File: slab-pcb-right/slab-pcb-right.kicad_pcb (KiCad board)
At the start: 2 copper layers, 158 x 104 mm, 147 parts, among them J1 Conn_01x04, J2 Conn_01x04, J3 TRRS_L, J4 TRRS_R, J5 SSD1306, SW1 RotaryEncoder, U1 Seeeduino Xiao rp2040, U2 PCA9555PW, U3 PCA9555PW, U4 ADS1110, U5 SN74AHCT125PWR, U6 TCA4307DGKR

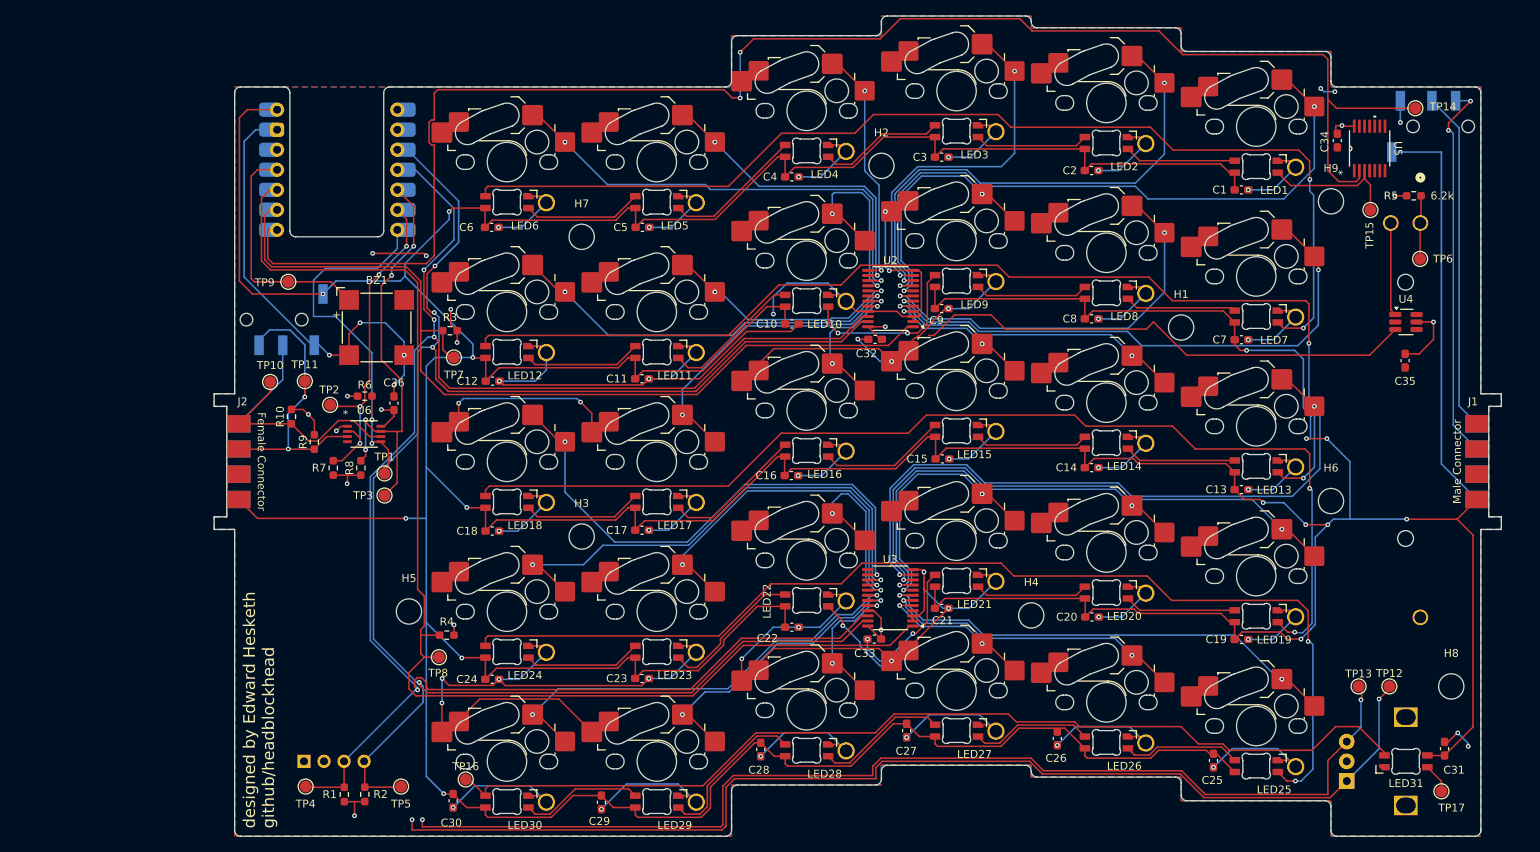
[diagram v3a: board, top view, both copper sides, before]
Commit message: feat: restart slab-pcb-right routing, allign components
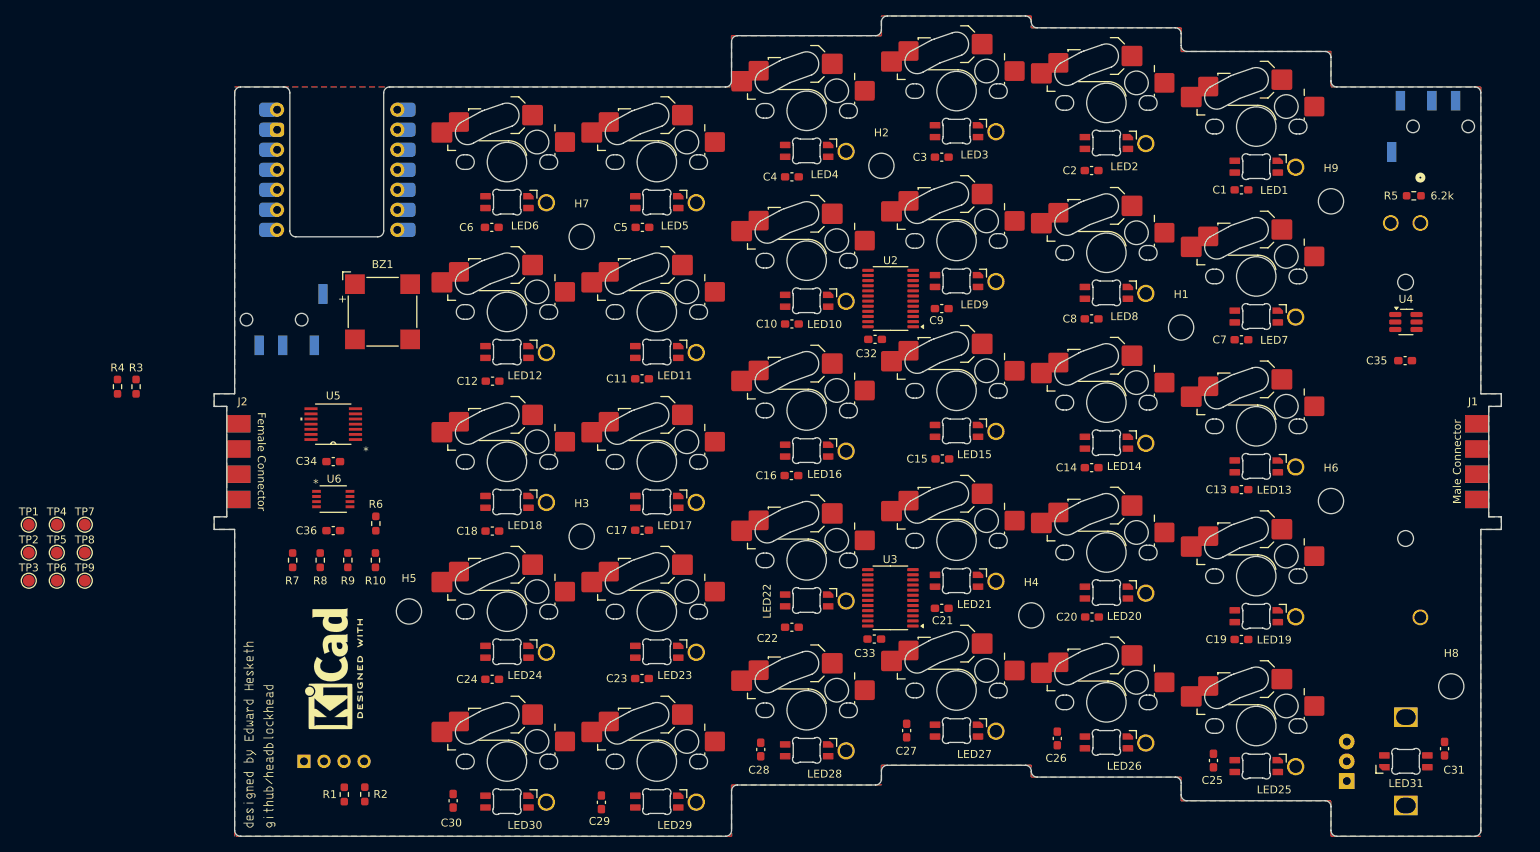
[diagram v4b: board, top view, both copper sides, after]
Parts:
- removed TP10, TP11, TP12, TP13, TP14, TP15, TP16, TP17: TestPoint, TestPoint:TestPoint_Pad_D1.5mm
- added REF**: KiCad-Logo2_6mm_SilkScreen, Symbol:KiCad-Logo2_6mm_SilkScreen, F.Cu at (81.9, 128.8)
- moved TP6 177.6 mm to (47.5, 117.6)
- moved U5 136.0 mm to (82.5, 97.8), turned to 180 degrees
- moved C34 133.6 mm to (82.5, 102.5), turned to 0 degrees
- moved TP5 52.8 mm to (47.5, 114.0)
- moved R4 52.3 mm to (55.1, 93.0), turned to 90 degrees
- moved TP7 51.4 mm to (51.0, 110.5)
- moved TP8 46.8 mm to (51.0, 114.0)
- moved TP3 46.4 mm to (43.9, 117.6)
- moved TP9 45.8 mm to (51.0, 117.6)
- moved TP4 45.8 mm to (47.5, 110.5)
- moved TP1 45.6 mm to (43.9, 110.5)
- moved TP2 42.6 mm to (43.9, 114.0)
- moved R3 40.4 mm to (57.5, 93.0), turned to 90 degrees
- moved R10 21.1 mm to (87.8, 115.0), turned to -90 degrees
- moved C36 17.9 mm to (82.5, 111.2), turned to 0 degrees
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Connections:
- TP1 pad 1: /I2C1_RDY -> /SHIFTER_INPUT
- TP2 pad 1: /I2C1_SCL -> /SHIFTER_OUTPUT
- TP3 pad 1: /I2C1_SDA -> Net-(R5-Pad2)
- TP4 pad 1: /I2C0_SCL -> /RGBLEDARRAY_OUTPUT
- TP5 pad 1: /I2C0_SDA -> Net-(LED31-DOUT)
- TP6 pad 1: Net-(R5-Pad2) -> /ROT_B
- TP7 pad 1: /EXPANDER1_INT -> /ROT_A
- TP8 pad 1: /EXPANDER2_INT -> /I2C0_SCL
- TP9 pad 1: /BUZZER -> /I2C0_SDA
- U1 pad 12: /EXPANDER2_INT -> /SHIFTER_INPUT
- U1 pad 13: /EXPANDER1_INT -> /EXPANDER2_INT
- U1 pad 14: /SHIFTER_INPUT -> /EXPANDER1_INT
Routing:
- net VBUS: track 920.7 -> 0.00 mm, vias 15 -> 0
- net GND: track 659.3 -> 0.00 mm, vias 51 -> 0
- net /I2C0_SCL: track 292.4 -> 0.00 mm, vias 4 -> 0
- net /I2C0_SDA: track 226.7 -> 0.00 mm, vias 4 -> 0
- net /SHIFTER_INPUT: track 203.3 -> 0.00 mm, vias 2 -> 0
- net /EXPANDER2_INT: track 156.5 -> 0.00 mm
- net /ROT_A: track 144.1 -> 0.00 mm, vias 2 -> 0
- net /ROT_B: track 140.4 -> 0.00 mm, vias 2 -> 0
- net Net-(LED18-DOUT): track 138.3 -> 0.00 mm, vias 2 -> 0
- net Net-(LED12-DOUT): track 137.8 -> 0.00 mm, vias 2 -> 0
- net Net-(LED24-DOUT): track 137.7 -> 0.00 mm, vias 2 -> 0
- net Net-(LED6-DOUT): track 137.3 -> 0.00 mm, vias 2 -> 0
- net /RGBLEDARRAY_OUTPUT: track 127.0 -> 0.00 mm
- net /EXPANDER1_INT: track 114.0 -> 0.00 mm
- net /I2C_BUS_SCL: track 87.1 -> 0.00 mm, vias 4 -> 0
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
